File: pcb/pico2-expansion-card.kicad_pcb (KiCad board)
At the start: 2 copper layers, 26 x 30.6 mm, 52 parts, among them J3 Conn_01x03_Socket, J4 Conn_01x04_Socket, Q1 EM6K6, Q2 EM6K6, SW1 SW_Push, U2 RP2354A, U4 AP2127K-3.3, Y1 ABM8-272-T3

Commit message: edit pcb more, polish it
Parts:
- moved C12 10.5 mm to (103.4, 68.2)
- moved C11 1.29 mm to (111.0, 71.5)
- moved C9 1.19 mm to (110.0, 71.5)
- moved R9 0.20 mm to (115.8, 79.6)
- moved R6 0.09 mm to (113.6, 79.6)
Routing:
- net +3.3V: track 116.7 -> 114.6 mm
- net GND: track 7.01 -> 7.30 mm, vias 33 -> 36

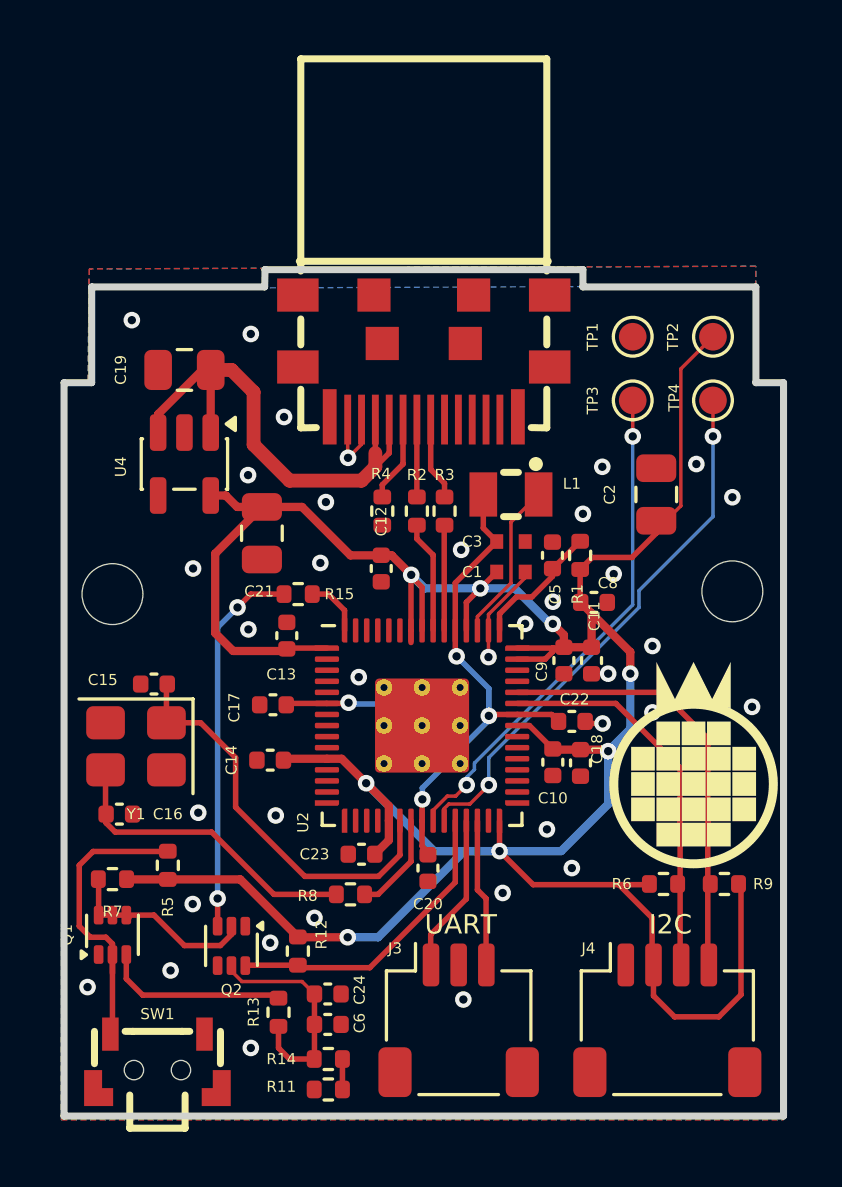
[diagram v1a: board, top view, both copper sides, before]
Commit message: fix hole positions
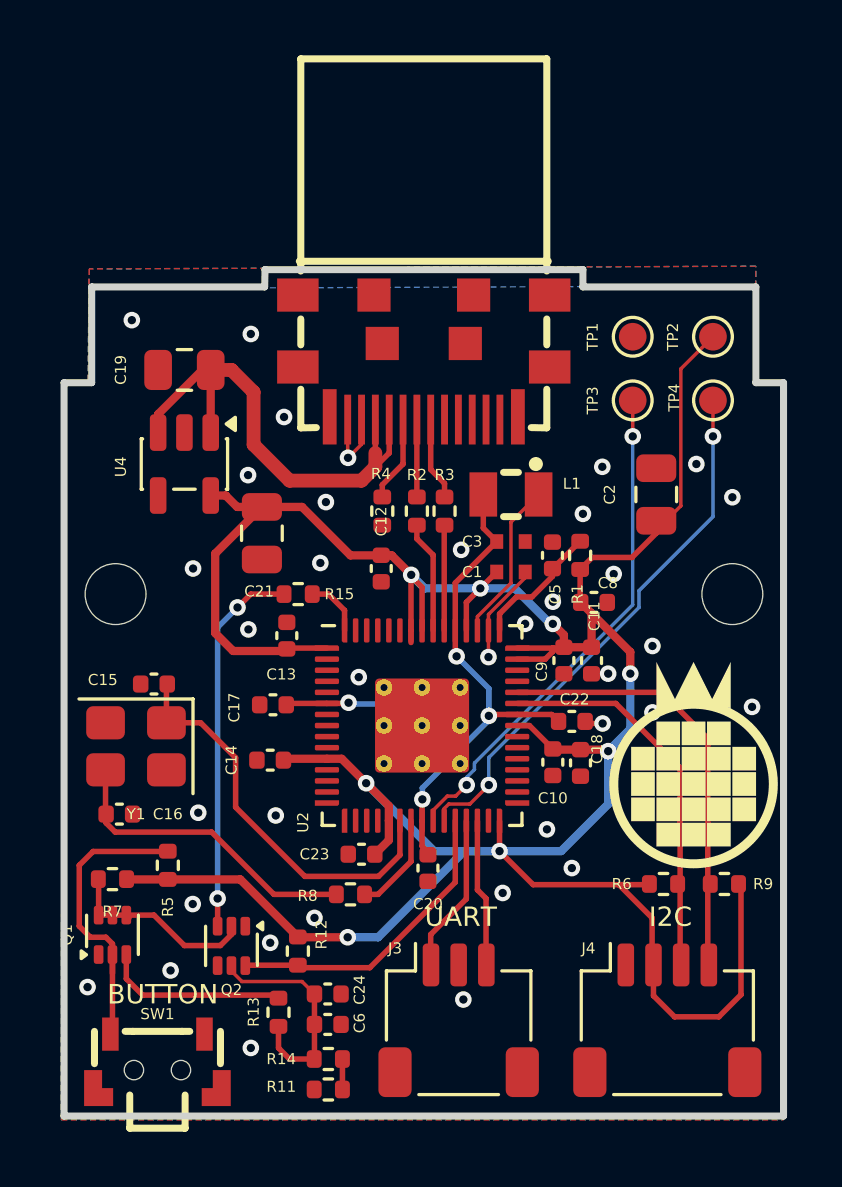
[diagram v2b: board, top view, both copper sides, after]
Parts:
- moved H1 0.11 mm to (93.8, 69.1)

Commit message: minor cleanup after dfn check
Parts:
- moved C2 0.44 mm to (113.0, 65.8)
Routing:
- net GND: track 7.30 -> 4.64 mm, vias 36 -> 33
- net +3.3V: track 114.6 -> 113.6 mm
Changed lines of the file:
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@@
 	(footprint "Capacitor_SMD:C_0805_2012Metric"
 		(layer "F.Cu")
-		(at 113.3375 65.525 90)
+		(at 113 65.8 90)
 		(descr "Capacitor SMD 0805 (2012 Metric), square (rectangular) end terminal, IPC-7351 nominal, (Body size source: IPC-SM-782 page 76, https://www.pcb-3d.com/wordpress/wp-content/uploads/ipc-sm-782a_amendment_1_and_2.pdf, https://docs.google.com/spreadsheets/d/1BsfQQcO9C6DZCsRaXUlFlo91Tg2WpOkGARC1WS5S8t0/edit?usp=sharing)")
 		(tags "capacitor")
@@
 	)
 	(segment
-		(start 108.6025 68.531026)
-		(end 108.6025 68.325)
-		(width 0.127)
-		(layer "F.Cu")
-		(net "GND")
-	)
-	(segment
 		(start 95.2675 75.555)
 		(end 95.2375 75.525)
@@
 	)
 	(segment
-		(start 107.275 69.858526)
-		(end 108.6025 68.531026)
-		(width 0.127)
-		(layer "F.Cu")
-		(net "GND")
-	)
-	(segment
 		(start 102.68755 62.8185)
 		(end 102.68755 63.71245)
@@
 	)
 	(segment
-		(start 107.275 70.4375)
-		(end 107.275 69.858526)
-		(width 0.127)
-		(layer "F.Cu")
-		(net "GND")
-	)
-	(segment
 		(start 110.8425 73.8)
 		(end 110.7675 73.725)
@@
 	)
 	(via
-		(at 113.2 73.4)
-		(size 0.6)
-		(drill 0.3)
-		(layers "F.Cu" "B.Cu")
-		(free yes)
-		(net "GND")
-	)
-	(via
 		(at 111.6 72)
 		(size 0.6)
@@
 	)
 	(via
-		(at 109.6 69.4)
-		(size 0.6)
-		(drill 0.3)
-		(layers "F.Cu" "B.Cu")
-		(free yes)
-		(net "GND")
-	)
-	(via
-		(at 108.6 70.2)
-		(size 0.6)
-		(drill 0.3)
-		(layers "F.Cu" "B.Cu")
-		(free yes)
-		(net "GND")
-	)
-	(via
 		(at 101.4 65.8)
 		(size 0.6)
@@
 	)
 	(via
-		(at 111.4 73.8)
+		(at 109.7 69.3)
 		(size 0.6)
 		(drill 0.3)
@@
 	)
 	(via
-		(at 99.5875 77.125)
+		(at 111.4 73.8)
 		(size 0.6)
 		(drill 0.3)
@@
 	)
 	(via
-		(at 98.6 70.4)
+		(at 99.5875 77.125)
 		(size 0.6)
 		(drill 0.3)
@@
 	)
 	(via
-		(at 96.6 68.2)
+		(at 98.6 70.4)
 		(size 0.6)
 		(drill 0.3)
@@
 	)
 	(via
-		(at 116.0875 65.625)
+		(at 96.6 68.2)
 		(size 0.6)
 		(drill 0.3)
@@
 	)
 	(via
-		(at 114.7875 64.425)
+		(at 116.0875 65.625)
 		(size 0.6)
 		(drill 0.3)
@@
 	)
 	(segment
+		(start 112.0725 66.75)
+		(end 113 66.75)
+		(width 0.3)
+		(layer "F.Cu")
+		(net "+3.3V")
+	)
+	(segment
+		(start 114.2 61.0125)
+		(end 115.3875 59.825)
+		(width 0.3)
+		(layer "F.Cu")
+		(net "+3.3V")
+	)
+	(segment
 		(start 104.482977 68.429523)
 		(end 103.778455 67.725)
@@
 	)
 	(segment
-		(start 112.4625 67.8)
-		(end 113.3375 66.925)
-		(width 0.2)
-		(layer "F.Cu")
-		(net "+3.3V")
-	)
-	(segment
 		(start 109.6 71.2)
 		(end 109.6 71.075)
@@
 	)
 	(segment
-		(start 113.3375 66.825)
-		(end 114.226 65.9365)
-		(width 0.127)
-		(layer "F.Cu")
-		(net "+3.3V")
-	)
-	(segment
 		(start 106.475 69.4225)
 		(end 106.475 70.425)
@@
 	)
 	(segment
-		(start 110.5875 68.235)
-		(end 111.0225 67.8)
-		(width 0.2)
-		(layer "F.Cu")
-		(net "+3.3V")
-	)
-	(segment
 		(start 109.6 70.2)
 		(end 110 70.6)
@@
 	)
 	(segment
-		(start 113.3375 66.925)
-		(end 113.3375 66.475)
-		(width 0.2)
-		(layer "F.Cu")
-		(net "+3.3V")
-	)
-	(segment
 		(start 111.9875 79.625)
 		(end 112.975 79.625)
@@
 	)
 	(segment
-		(start 111.0225 67.8)
-		(end 112.4625 67.8)
-		(width 0.2)
-		(layer "F.Cu")
-		(net "+3.3V")
-	)
-	(segment
 		(start 114 84.4)
 		(end 115.6 84.4)
@@
 	)
 	(segment
+		(start 110.5875 68.235)
+		(end 112.0725 66.75)
+		(width 0.3)
+		(layer "F.Cu")
+		(net "+3.3V")
+	)
+	(segment
 		(start 108.8875 79.625)
 		(end 107.675 78.4125)
@@
 	)
 	(segment
-		(start 114.226 60.9865)
-		(end 115.3875 59.825)
-		(width 0.127)
-		(layer "F.Cu")
-		(net "+3.3V")
-	)
-	(segment
 		(start 102.1875 81.525)
 		(end 100.3275 81.525)
@@
 	)
 	(segment
+		(start 114.2 65.55)
+		(end 114.2 61.0125)
+		(width 0.3)
+		(layer "F.Cu")
+		(net "+3.3V")
+	)
+	(segment
 		(start 116.4 79.71)
 		(end 116.31 79.62)
@@
 	)
 	(segment
+		(start 113 66.75)
+		(end 114.2 65.55)
+		(width 0.3)
+		(layer "F.Cu")
+		(net "+3.3V")
+	)
+	(segment
 		(start 113.1875 82.525)
 		(end 113.1875 80.825)
@@
 	)
 	(segment
-		(start 104.475 70.4375)
-		(end 104.475 70.875)
-		(width 0.2)
-		(layer "F.Cu")
-		(net "+3.3V")
-	)
-	(segment
 		(start 97.4 67.6625)
 		(end 99.0875 65.975)
@@
 	)
 	(segment
-		(start 114.226 65.9365)
-		(end 114.226 60.9865)
-		(width 0.127)
-		(layer "F.Cu")
-		(net "+3.3V")
-	)
-	(segment
 		(start 108.3125 71.475)
 		(end 109.325 71.475)
@@
 	)
 	(segment
-		(start 109.5875 68.484999)
-		(end 108.847499 69.225)
+		(start 107.675 70.225)
+		(end 107.675 70.4375)
 		(width 0.2)
 		(layer "F.Cu")
@@
 	)
 	(segment
-		(start 108.2875 69.225)
-		(end 107.675 69.8375)
-		(width 0.2)
-		(layer "F.Cu")
-		(net "/VREG_AVDD")
-	)
-	(segment
-		(start 108.847499 69.225)
-		(end 108.2875 69.225)
+		(start 109.5875 68.3125)
+		(end 107.675 70.225)
 		(width 0.2)
 		(layer "F.Cu")
@@
 	)
 	(segment
-		(start 107.675 69.8375)
-		(end 107.675 70.425)
-		(width 0.2)
-		(layer "F.Cu")
-		(net "/VREG_AVDD")
-	)
-	(segment
 		(start 109.5875 68.205)
-		(end 109.5875 68.484999)
+		(end 109.5875 68.3125)
 		(width 0.2)
 		(layer "F.Cu")
@@
 	)
 	(segment
-		(start 106.875 69.9375)
-		(end 108.0875 68.725)
+		(start 108.0875 68.6125)
+		(end 108.0875 66.525)
 		(width 0.127)
 		(layer "F.Cu")
@@
 	)
 	(segment
-		(start 106.875 70.4375)
-		(end 106.875 69.9375)
+		(start 108.0875 66.525)
+		(end 109.0875 65.525)
 		(width 0.127)
 		(layer "F.Cu")
@@
 	)
 	(segment
-		(start 108.0875 66.525)
-		(end 109.0875 65.525)
+		(start 106.875 70.4375)
+		(end 106.875 69.825)
 		(width 0.127)
 		(layer "F.Cu")
@@
 	)
 	(segment
-		(start 108.0875 68.725)
-		(end 108.0875 66.525)
+		(start 106.875 69.825)
+		(end 108.0875 68.6125)
 		(width 0.127)
 		(layer "F.Cu")

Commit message: fix false UART
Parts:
- J3: value Conn_01x03_Socket -> Conn_01x04_Socket; footprint Connector_JST:JST_SH_SM03B-SRSS-TB_1x03-1MP_P1.00mm_Horizontal -> Connector_JST:JST_SH_SM04B-SRSS-TB_1x04-1MP_P1.00mm_Horizontal
- moved C24 0.59 mm to (100.9, 83.5)
- moved R13 0.59 mm to (99.1, 84.2)
- moved C6 0.59 mm to (100.9, 84.7)
- moved R11 0.59 mm to (100.9, 87.0)
- moved R14 0.59 mm to (100.9, 85.9)
- moved J3 0.30 mm to (105.9, 84.5)
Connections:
- J3 pad 1: /GPIO16/TX -> GND
- J3 pad 2: GND -> +3.3V
- J3 pad 3: /GPIO17/RX -> /GPIO16/TX
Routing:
- net +3.3V: track 113.6 -> 116.8 mm, vias 8 -> 9
- net Net-(Q1B-D): track 6.62 -> 6.07 mm
- net /GPIO16/TX: track 5.73 -> 5.21 mm
- net Net-(Q2B-G): track 8.13 -> 7.61 mm
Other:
- board text added: "BOOT"
- board text added: "License: CERN-OHL-S v2 Version: 0.2.0p (Prototype)"
- board text removed: "BUTTON"
- board text removed: "License: CERN-OHL-S v2 Version: 0.1.0p (Prototype)"
- board text removed: "riscfruit.com"
